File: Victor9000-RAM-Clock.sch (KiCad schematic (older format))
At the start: 18 parts, among them U1 74LS00, U2 74LS11, U3 74LS139, U4 74LS373, U5 AS6C4008-55PCN, U6 74LS245, U7 AS6C4008-55PCN

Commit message: Routing completed
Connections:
- wire segments 224 -> 232
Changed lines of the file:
@@
 Title "Victor 9000 RAM Expansion"
 Date ""
-Rev ""
+Rev "v01"
 Comp ""
 Comment1 ""
@@
 P 1600 3850
 F 0 "H1" H 3000 3550 50  0001 C CNN
-F 1 "Expansion_Connector" H 1600 2350 50  0000 C CNN
+F 1 "Expansion_Connector" H 1600 2000 50  0000 C CNN
 F 2 "victor-exp:Victor Expansion Edge Connector" H 2450 4050 50  0001 C CNN
 F 3 "" H 2450 4050 50  0001 C CNN
@@
 L power:GND #PWR02
 U 1 1 61FD5D7E
-P 2550 5200
-F 0 "#PWR02" H 2550 4950 50  0001 C CNN
-F 1 "GND" H 2555 5027 50  0000 C CNN
-F 2 "" H 2550 5200 50  0001 C CNN
-F 3 "" H 2550 5200 50  0001 C CNN
-	1    2550 5200
-	1    0    0    -1
-$EndComp
-Wire Wire Line
-	2100 5150 2550 5150
-Wire Wire Line
-	2550 5150 2550 5200
+P 2550 5600
+F 0 "#PWR02" H 2550 5350 50  0001 C CNN
+F 1 "GND" H 2555 5427 50  0000 C CNN
+F 2 "" H 2550 5600 50  0001 C CNN
+F 3 "" H 2550 5600 50  0001 C CNN
+	1    2550 5600
+	1    0    0    -1
+$EndComp
 Wire Wire Line
 	2100 4850 2550 4850
@@
 NoConn ~ 1050 4650
 NoConn ~ 1050 4750
-NoConn ~ 2100 4950
 NoConn ~ 2100 5050
 NoConn ~ 4800 1900
@@
 	1    0    0    1
 $EndComp
+NoConn ~ 2100 5150
+Wire Wire Line
+	2100 4950 2550 4950
+Wire Wire Line
+	2550 4950 2550 4850
+Connection ~ 2550 4850
+Wire Wire Line
+	2100 5250 2550 5250
+Wire Wire Line
+	2550 5250 2550 5350
+Wire Wire Line
+	2100 5350 2550 5350
+Connection ~ 2550 5350
+Wire Wire Line
+	2550 5350 2550 5450
+Wire Wire Line
+	2100 5450 2550 5450
+Connection ~ 2550 5450
+Wire Wire Line
+	2550 5450 2550 5550
+Wire Wire Line
+	2100 5550 2550 5550
+Connection ~ 2550 5550
+Wire Wire Line
+	2550 5550 2550 5600
 $EndSCHEMATC

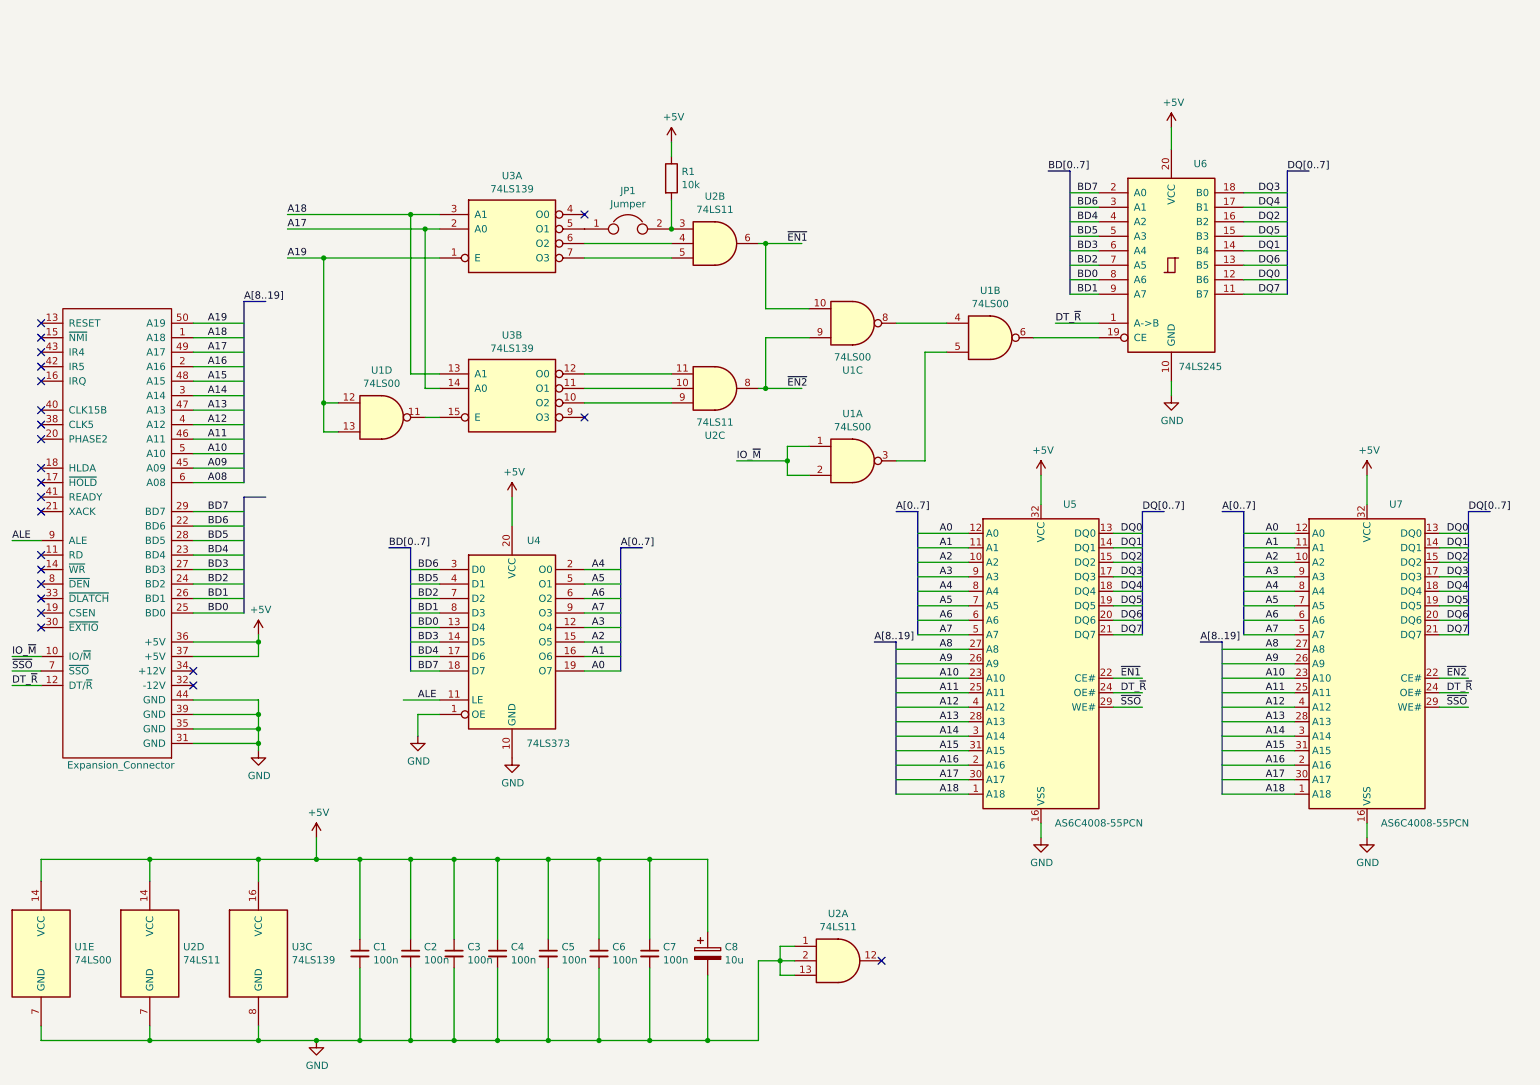
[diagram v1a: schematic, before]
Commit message: DS1315 added
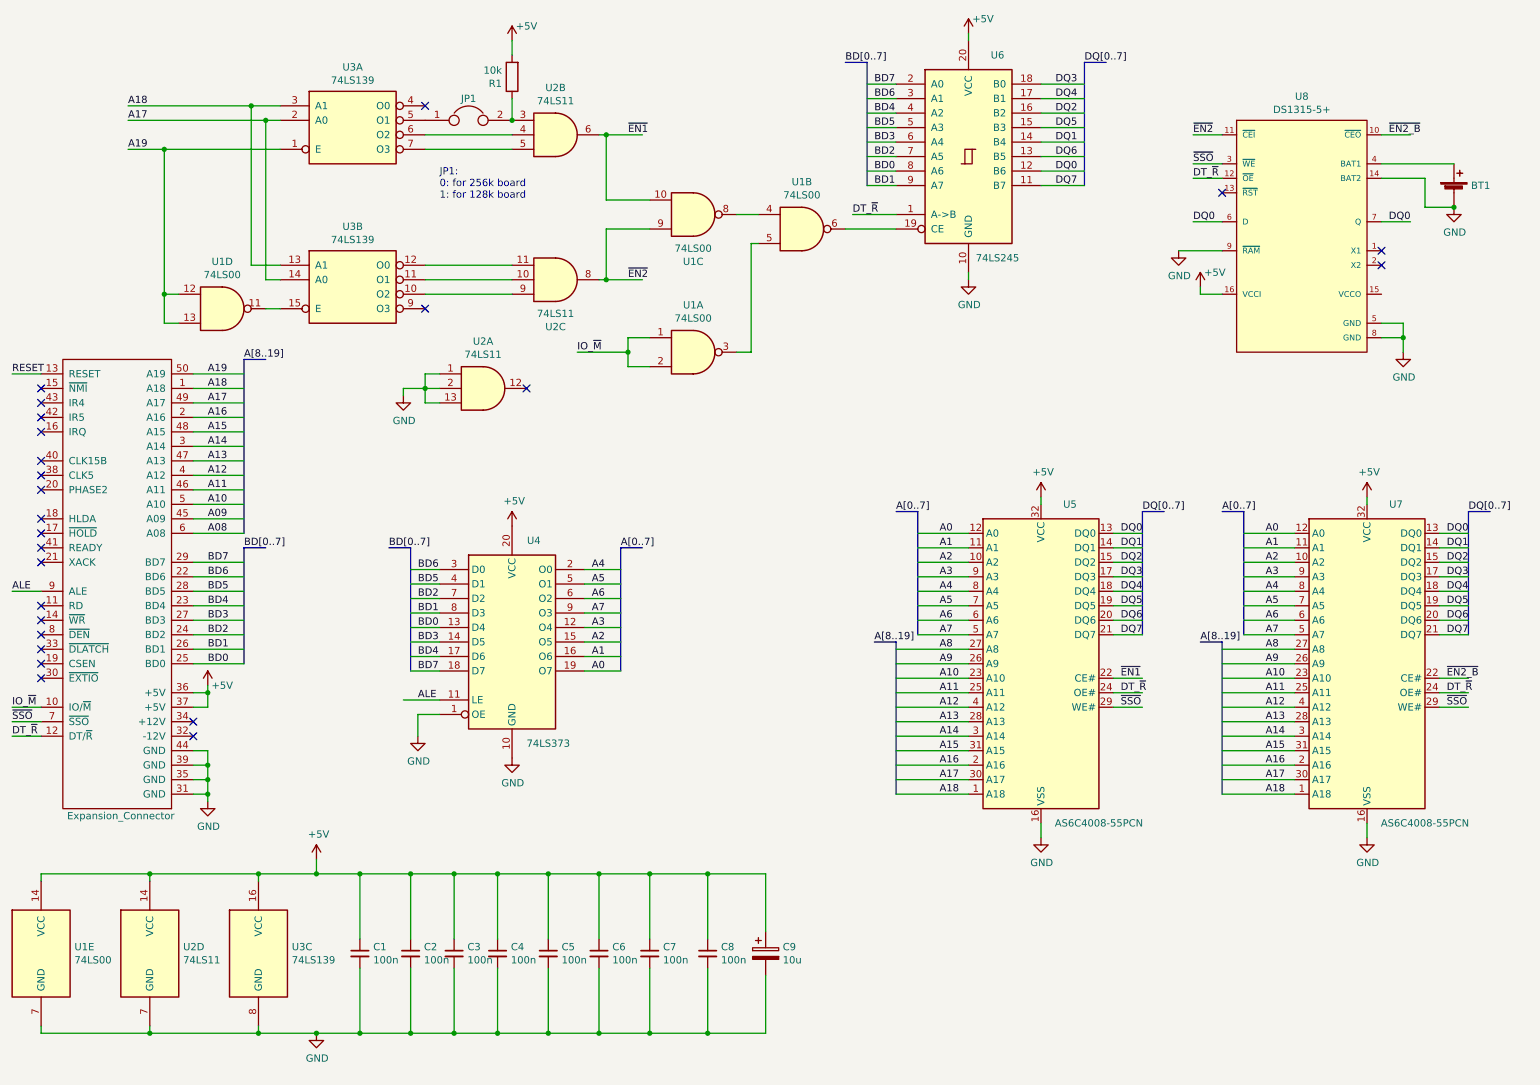
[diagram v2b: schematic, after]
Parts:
- added BT1: Battery_Cell, Battery:BatteryHolder_Keystone_103_1x20mm, symbol Device:Battery_Cell
- added C8: 100n, Capacitor_THT:C_Disc_D5.0mm_W2.5mm_P2.50mm, symbol Device:C_Small
- added U8: DS1315-5+, eec:Maxim-DS1315-5+-Manufacturer_Recommended, symbol eec:DS1315-5+
- renumbered C8 to C9
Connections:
- net labels added: RESET, ~EN2_B
- wire segments 232 -> 252
- no-connect marks 23 -> 25
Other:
- note added: "JP1:\n0: for 256k board\n1: for 128k board"
- moved on the sheet: C9, JP1, R1, U1A, U1B, U1C, U1D, U2A, U2B, U2C, U3A, U3B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

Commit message: Comments added
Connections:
- wire segments 252 -> 253
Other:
- note added: "20000h /\n40000h - 70000h"
- note added: "80000h - D0000h"
- note added: "Mapped to \n80000h-D0000h"
- note added: "unused"
- moved on the sheet: BT1, JP1, R1, U1A, U1B, U1C, U1D, U2B, U2C, U3A, U3B, U4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
